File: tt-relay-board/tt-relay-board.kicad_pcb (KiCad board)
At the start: 2 copper layers, 85.1 x 48.3 mm, 16 parts, among them J1 AC_IN, J2 Screw_Terminal_01x02, J5 Conn_02x11_Odd_Even, J7 AudioJack4_SwitchR1, J8 AudioJack4_SwitchR1, Q1 Q_NPN_EBC

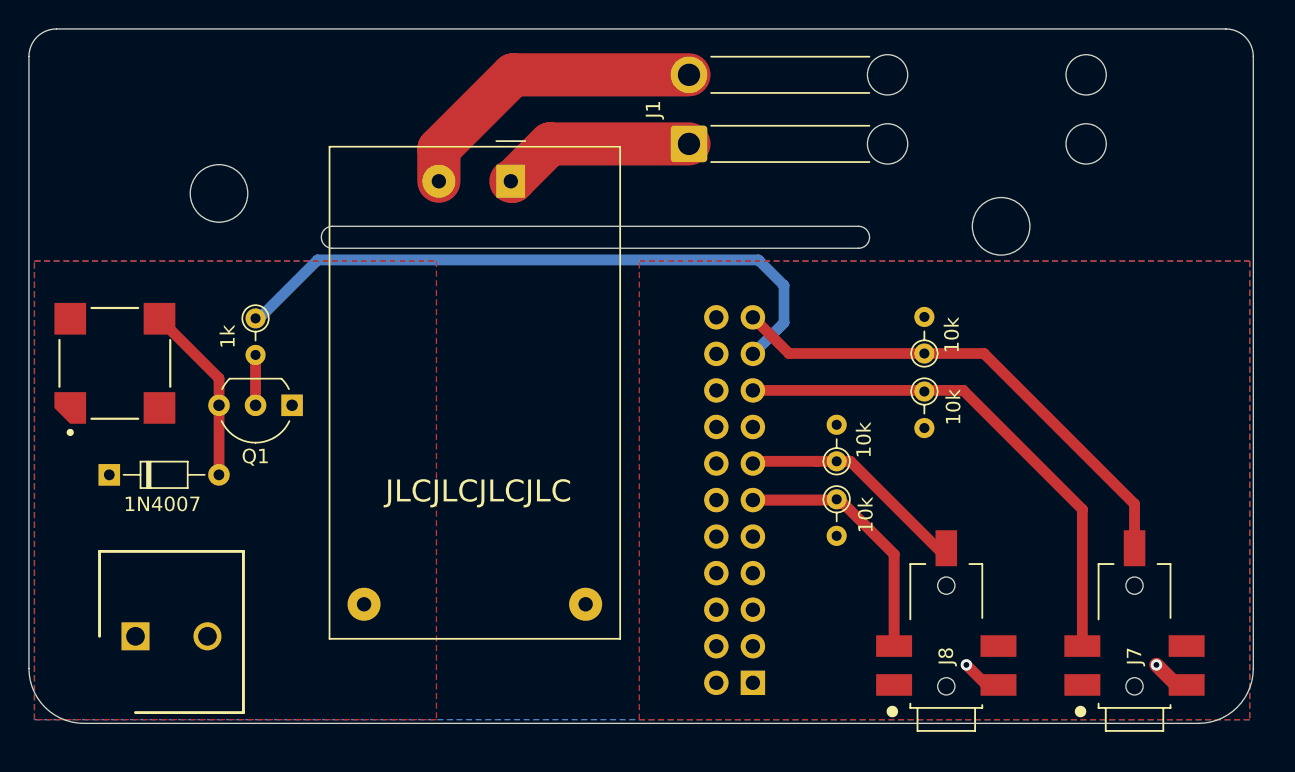
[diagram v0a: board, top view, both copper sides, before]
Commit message: Fix component positions in tt-relay-board
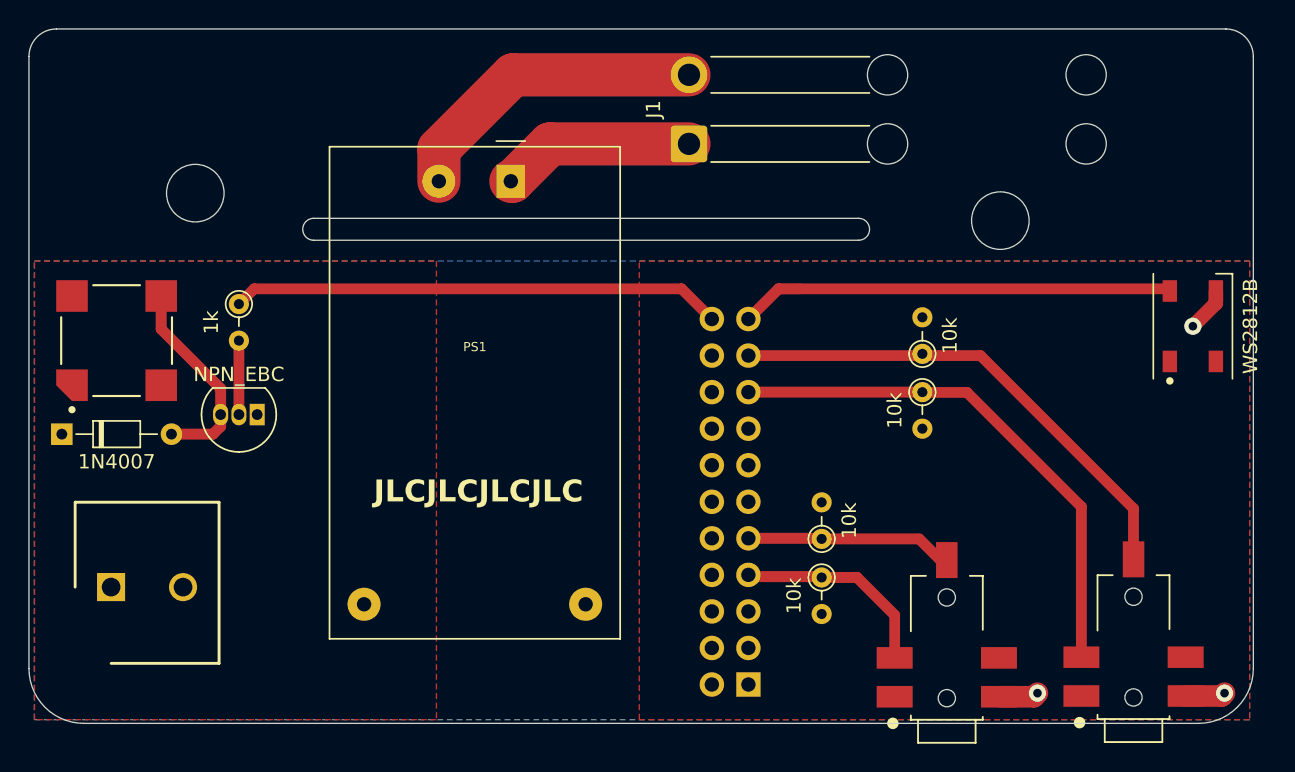
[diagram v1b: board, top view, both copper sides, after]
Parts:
- removed J7, J8: AudioJack4_SwitchR1, reptile-monitor:Korean Hroparts Elec PJ-227-5A
- added D2: 1N4007, Diode_THT:D_DO-34_SOD68_P7.62mm_Horizontal, F.Cu at (44.2, 81.5)
- added J3: Screw_Terminal_01x02, tt-relay-board:SHDR2W110P0X500_1X2_1000X1120X, F.Cu at (47.6, 92.1)
- added J4: AudioJack4_SwitchR1, tt-relay-board:Korean Hroparts Elec PJ-227-5A, F.Cu at (105.7, 101.3)
- D1: value 1N4007 -> WS2812B; footprint Diode_THT:D_DO-34_SOD68_P7.62mm_Horizontal -> tt-relay-board:LED_WS2812B_PLCC4_5.0x5.0mm_P3.2mm
- J2: value Screw_Terminal_01x02 -> AudioJack4_SwitchR1; footprint tt-relay-board:SHDR2W110P0X500_1X2_1000X1120X -> tt-relay-board:Korean Hroparts Elec PJ-227-5A
- LS1: footprint reptile-monitor:Mallory_Sonalert_Products_Inc-AST7525MATRQ-0-0-MFG -> tt-relay-board:Mallory_Sonalert_Products_Inc-AST7525MATRQ-0-0-MFG
- PS1: footprint reptile-monitor-power:Converter_ACDC_HiLink_HLK-PMxx -> tt-relay-board:Converter_ACDC_HiLink_HLK-PMxx
- Q1: value Q_NPN_EBC -> NPN_EBC; footprint Package_TO_SOT_THT:TO-92_Inline_Wide -> Package_TO_SOT_THT:TO-92_Inline
- R1: value 1k -> 10k
- R5: value 10k -> 1k
- moved D1 76.0 mm to (122.8, 74.0), turned to 90 degrees
- moved J2 69.6 mm to (118.7, 101.3), turned to 90 degrees
- moved R1 43.3 mm to (97.0, 91.5)
- moved R5 43.0 mm to (56.5, 72.5), turned to -90 degrees
- moved R2 12.5 mm to (97.0, 88.8), turned to 90 degrees
- moved R3 9.54 mm to (104.0, 78.6)
- moved Q1 2.51 mm to (57.8, 80.1)
- moved H1 1.65 mm to (53.5, 64.8)
- moved LS1 1.59 mm to (48.0, 75.0)
- moved H2 0.40 mm to (109.4, 66.7)
- moved J5 0.33 mm to (91.9, 98.9)
- moved R4 0.14 mm to (104.0, 75.9)
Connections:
- net IO02/MISO renamed IO02
- net IO14/CLK renamed IO14
- D1 pad 1: +5V -> +3V3
- D1 pad 2: Net-(D1-Pad2) -> unconnected-(D1-DOUT-Pad2)
- J2 pad 1: +5V -> +3V3
- J2 pad 2: GND -> IO26
- J5 pad 7: IO15/MOSI -> IO15
- LS1 pad 4: Net-(D1-Pad2) -> Net-(D2-A)
- Q1 pad 2: Net-(Q1-Pad2) -> Net-(Q1-B)
- Q1 pad 3: Net-(D1-Pad2) -> Net-(D2-A)
- R1 pad 1: IO26 -> IO15
- R1 pad 2: Net-(Q1-Pad2) -> +3V3
- R2 pad 1: IO13 -> IO12
- R3 pad 1: IO32 -> IO13
- R4 pad 1: IO22 -> IO26
- R5 pad 1: IO35 -> IO23
- R5 pad 2: +3V3 -> Net-(Q1-B)
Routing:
- net IO23: track 0.25 -> 34.0 mm
- net IO32: track 17.8 -> 0.00 mm
- net IO35: track 16.3 -> 0.00 mm
- net Net-(D2-A): track 0.00 -> 14.4 mm
- net IO12: track 0.00 -> 14.4 mm
- net IO15: track 0.00 -> 14.0 mm
- net Net-(D1-Pad2): track 12.6 -> 0.00 mm
- net IO26: track 44.5 -> 34.7 mm
- net Net-(Q1-B): track 0.00 -> 5.14 mm
- net IO22: track 35.0 -> 30.2 mm
- net GND: track 4.44 -> 8.67 mm, vias 2 -> 3
- net Net-(Q1-Pad2): track 3.50 -> 0.00 mm
- net IO13: track 35.8 -> 36.6 mm
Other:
- outline, holes or cut-outs redrawn
